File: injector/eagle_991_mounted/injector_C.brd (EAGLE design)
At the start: 34 x 35.8 mm, 28 parts, among them J4 ICSP, U1 ATA6631, U2 ATMEGA328, U3 ATA6631, X1 16MHz

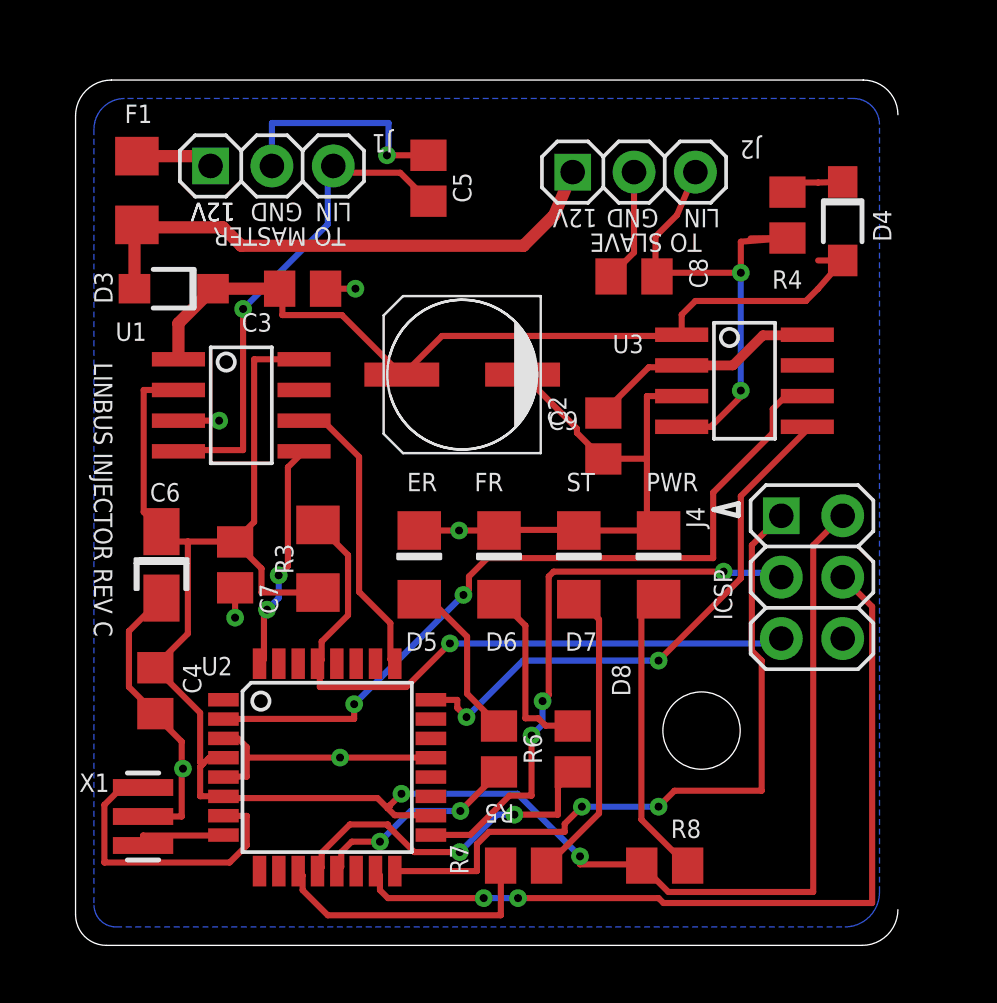
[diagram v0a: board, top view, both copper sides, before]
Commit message: new 991/981 board layout
- mounting hole position corrected
- added images of mounted board
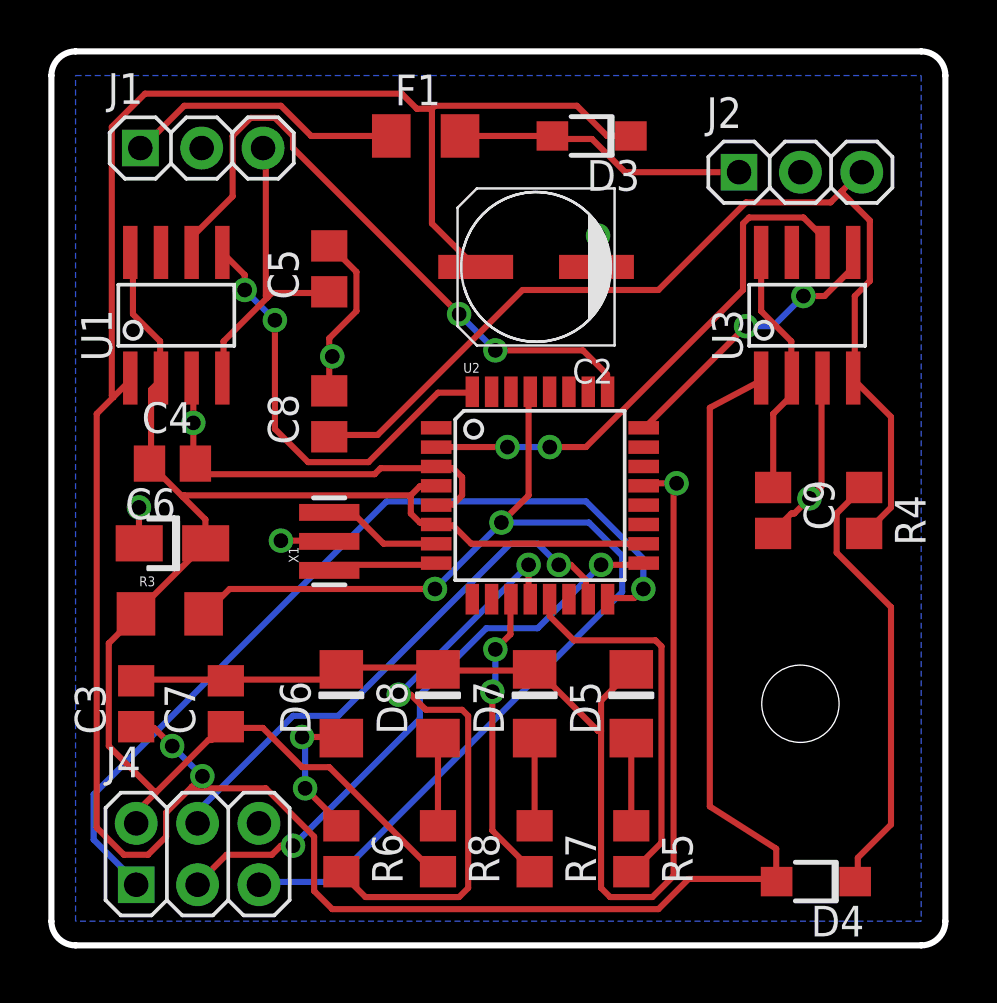
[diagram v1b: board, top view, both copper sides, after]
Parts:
- moved J4 27.9 mm to (5.05, 3.78), turned to 0 degrees
- moved D4 27.4 mm to (30.6, 2.64), turned to 180 degrees
- moved C3 18.5 mm to (2.51, 10.0), turned to 90 degrees
- moved D3 18.4 mm to (21.4, 33.5)
- moved U2 14.3 mm to (19.2, 18.6)
- moved C8 13.8 mm to (10.5, 22.0), turned to 90 degrees
- moved X1 13.7 mm to (10.5, 16.7)
- moved R4 12.6 mm to (32.6, 18.0)
- moved F1 12.2 mm to (14.5, 33.5), turned to 0 degrees
- moved D8 10.8 mm to (15.0, 10.0)
- moved D5 10.5 mm to (23.0, 10.0)
- moved R6 10.4 mm to (11.0, 4.00)
- moved C4 9.43 mm to (4.01, 19.9), turned to 0 degrees
- moved R8 9.41 mm to (15.0, 4.00), turned to 270 degrees
- moved D6 8.70 mm to (11.0, 10.0)
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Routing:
- net +12V: track 35.1 -> 122.7 mm, vias 0 -> 2
- net GND: track 65.7 -> 88.0 mm
- net LIN2: track 21.2 -> 42.7 mm, vias 2 -> 0
- net +5V: track 84.5 -> 65.1 mm, vias 2 -> 0
- net RESET: track 27.7 -> 47.0 mm, vias 1 -> 2
- net N$9: track 2.68 -> 18.4 mm
- net LIN1_TX: track 12.1 -> 26.7 mm, vias 0 -> 2
- net MOSI/LIN_ERR: track 35.5 -> 22.6 mm, vias 2 -> 1
- net LIN2_RX: track 23.1 -> 12.0 mm
- net FRAME_LED: track 14.3 -> 25.3 mm
- net N$6: track 22.8 -> 12.2 mm
- net LIN2_TX: track 32.5 -> 22.5 mm
- net N$1: track 12.3 -> 3.63 mm
- net LIN1_RX: track 9.56 -> 18.1 mm
- net N$2: track 12.1 -> 3.63 mm
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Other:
- board size 34 x 35.8 mm -> 37 x 37 mm
- board text removed: "12V"
- board text removed: "ER"
- board text removed: "FR"
- board text removed: "GND"
- board text removed: "ICSP"
- board text removed: "LIN"
- board text removed: "LINBUS INJECTOR - REV C"
- board text removed: "LINBUS INJECTOR REV C"
- board text removed: "PWR"
- board text removed: "ST"
- board text removed: "TO MASTER"
- board text removed: "TO SLAVE"
